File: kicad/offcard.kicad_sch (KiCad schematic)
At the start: 25 parts, among them J10 HeaderX4, J4 ScrewX2, J5 ScrewX4, J6 LCD, J7 HeaderX4, J8 ScrewX2, M1 12VDC motor, Q2 IRLML2502TRPbF, U3 NAU7802SGI

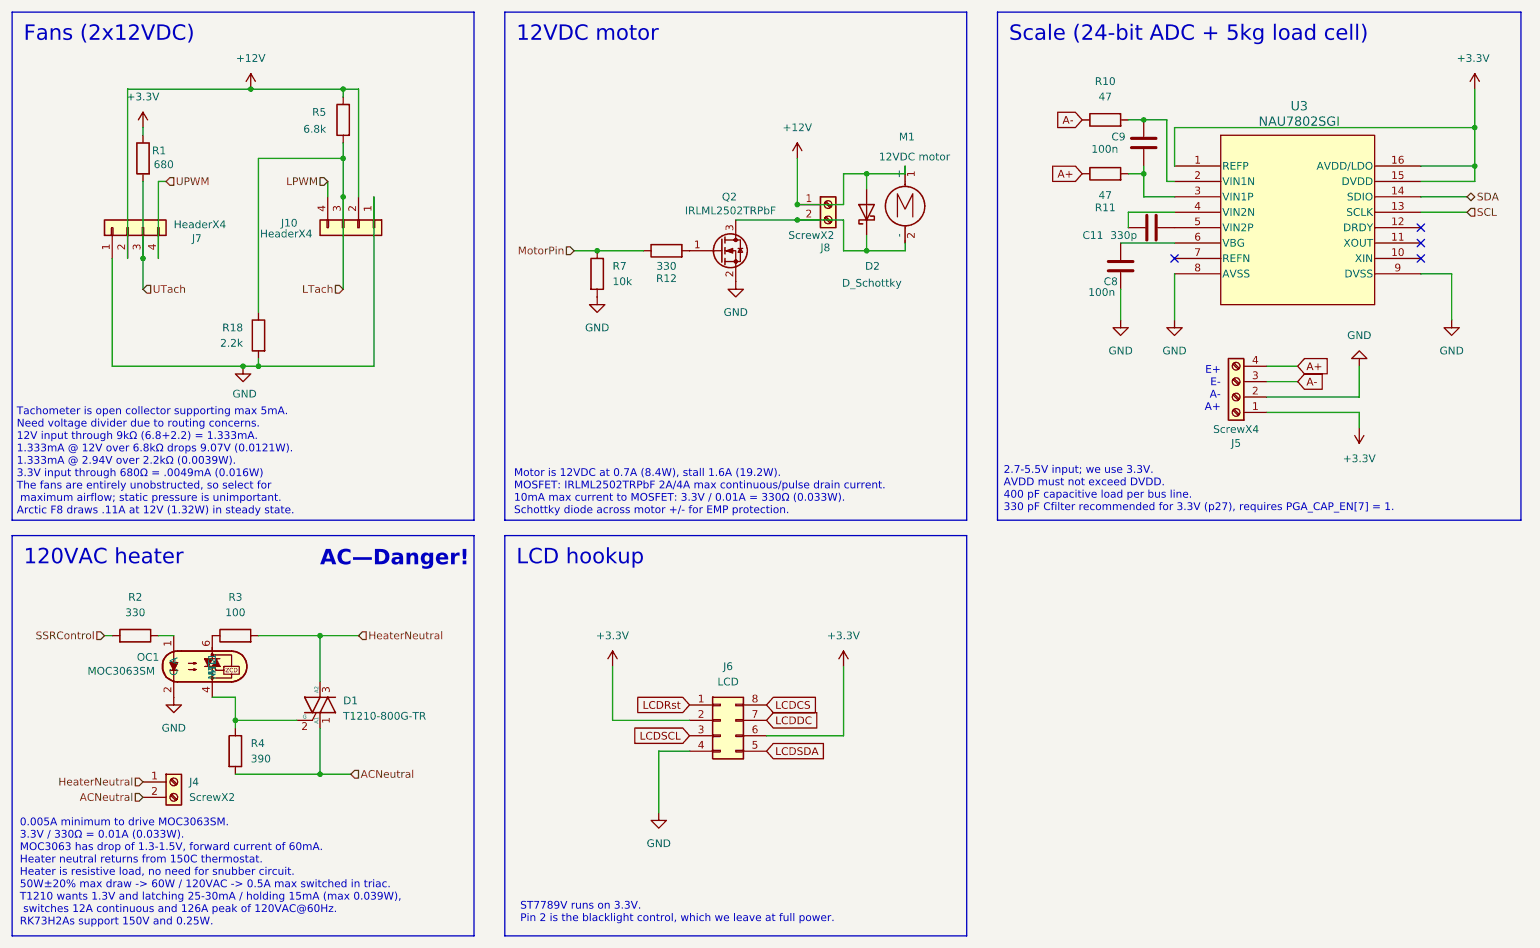
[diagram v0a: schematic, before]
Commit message: [nau7802] link avdd to refp, add capacitors #108
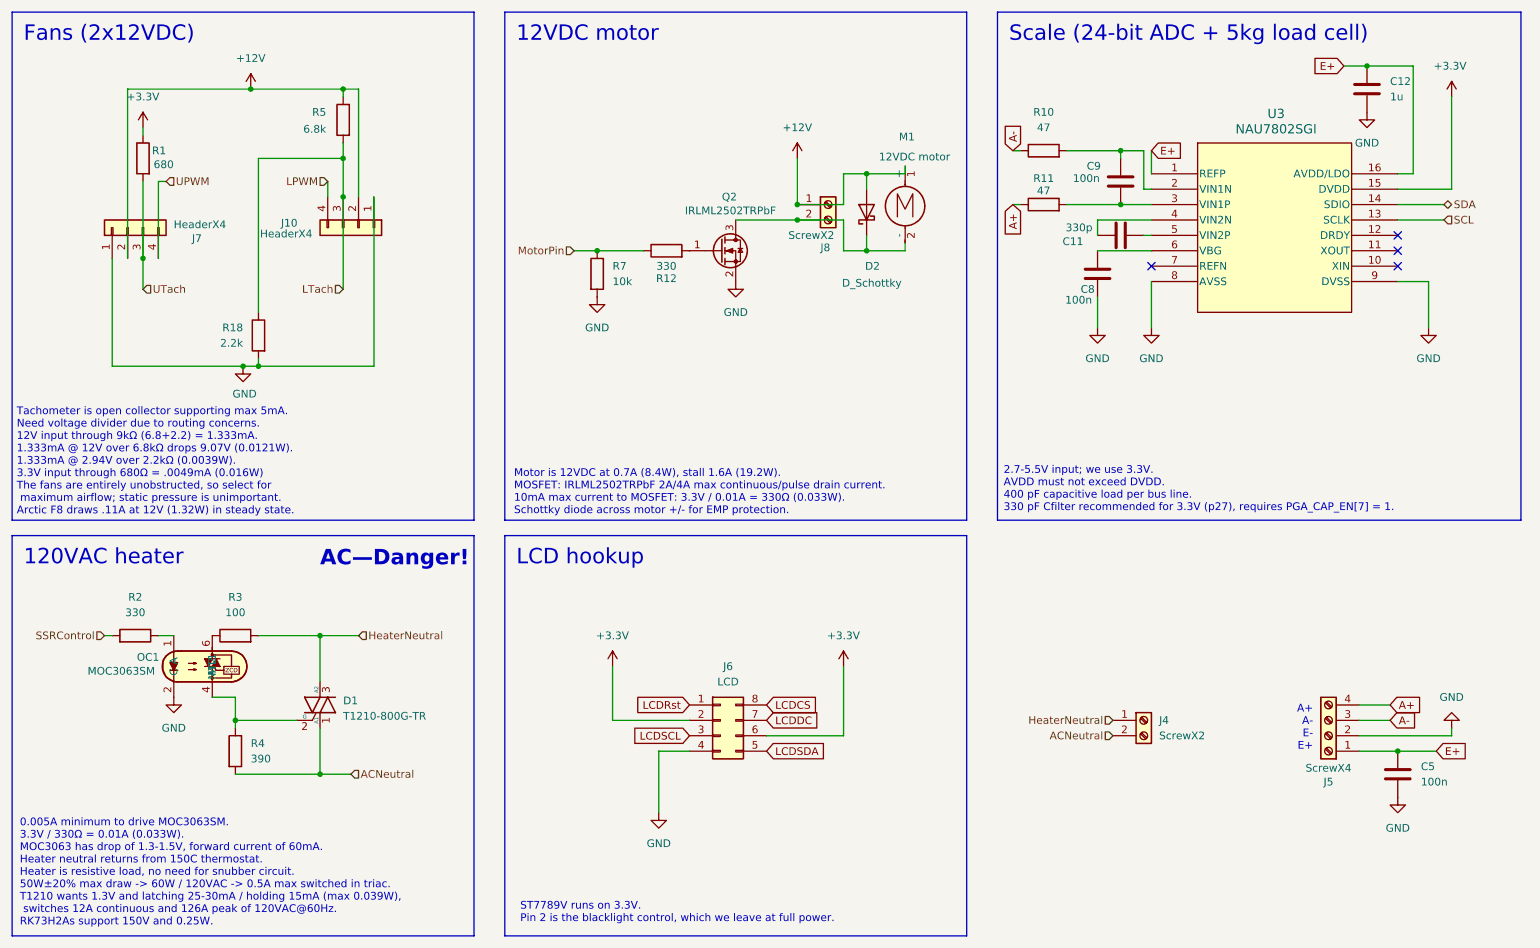
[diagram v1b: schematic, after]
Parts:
- added C12: 1u, Capacitor_SMD:C_1206_3216Metric_Pad1.33x1.80mm_HandSolder, symbol Device:C
- added C5: 100n, Capacitor_SMD:C_1206_3216Metric_Pad1.33x1.80mm_HandSolder, symbol Device:C
- R10, R11: footprint Resistor_SMD:R_0805_2012Metric_Pad1.20x1.40mm_HandSolder -> Resistor_SMD:R_1206_3216Metric_Pad1.30x1.75mm_HandSolder
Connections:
- net +3.3V: no longer J5.1 (Pin_1), U3.1 (REFP), U3.16 (AVDD/LDO)
- net GND: now also C12.2, C5.2
- new net E+: C12.1, C5.1, J5.1 (Pin_1), U3.1 (REFP), U3.16 (AVDD/LDO)
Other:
- note added: "A+ A- E- E+"
- note removed: "E+ E- A- A+"
- moved on the sheet: C11, C8, C9, J4, J5, R10, R11, U3

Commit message: move from lm35 to lmt87lpm
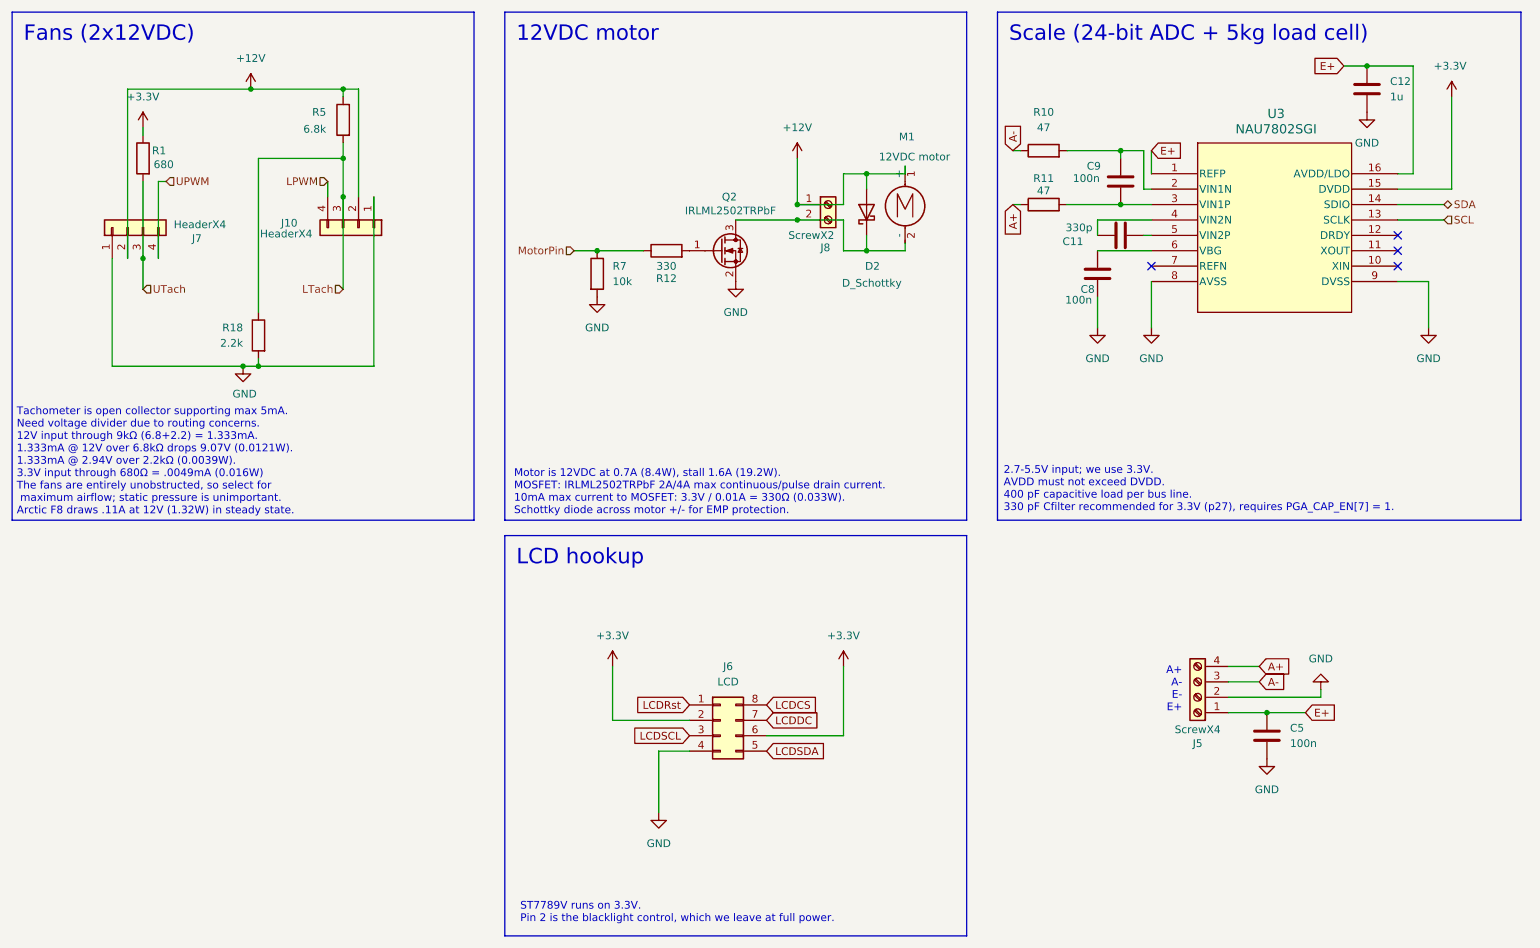
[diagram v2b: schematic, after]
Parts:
- removed D1: T1210-800G-TR, dank:T1210-800G-TR, symbol Triac_Thyristor:Generic_Triac_A1GA2
- removed J4: ScrewX2, TerminalBlock:TerminalBlock_bornier-2_P5.08mm, symbol Connector:Screw_Terminal_01x02
- removed OC1: MOC3063SM, dank:MOC306XS_LTO, symbol dank:MOC3063SM
- removed R2: 330, Resistor_SMD:R_1206_3216Metric_Pad1.30x1.75mm_HandSolder, symbol Device:R
- removed R3: 100, Resistor_SMD:R_1206_3216Metric_Pad1.30x1.75mm_HandSolder, symbol Device:R
- removed R4: 390, Resistor_SMD:R_1206_3216Metric_Pad1.30x1.75mm_HandSolder, symbol Device:R
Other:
- note removed: "0.005A minimum to drive MOC3063SM. 3.3V / 330Ω = 0.01A (0.033W). MOC3063 has drop of 1.3-1.5V, forward current of 60mA. Heater neutral returns from 150C thermostat. Heater is resistive load, no need for snubber circuit. 50W±20% max draw -> 60W / 120VAC -> 0.5A max switched in triac. T1210 wants 1.3V and latching 25-30mA / holding 15mA (max 0.039W), switches 12A continuous and 126A peak of 120VAC@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"
- note removed: "AC—Danger!"
- moved on the sheet: C5, J5

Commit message: [pcb] eliminate voltage divider before ltach closes #112
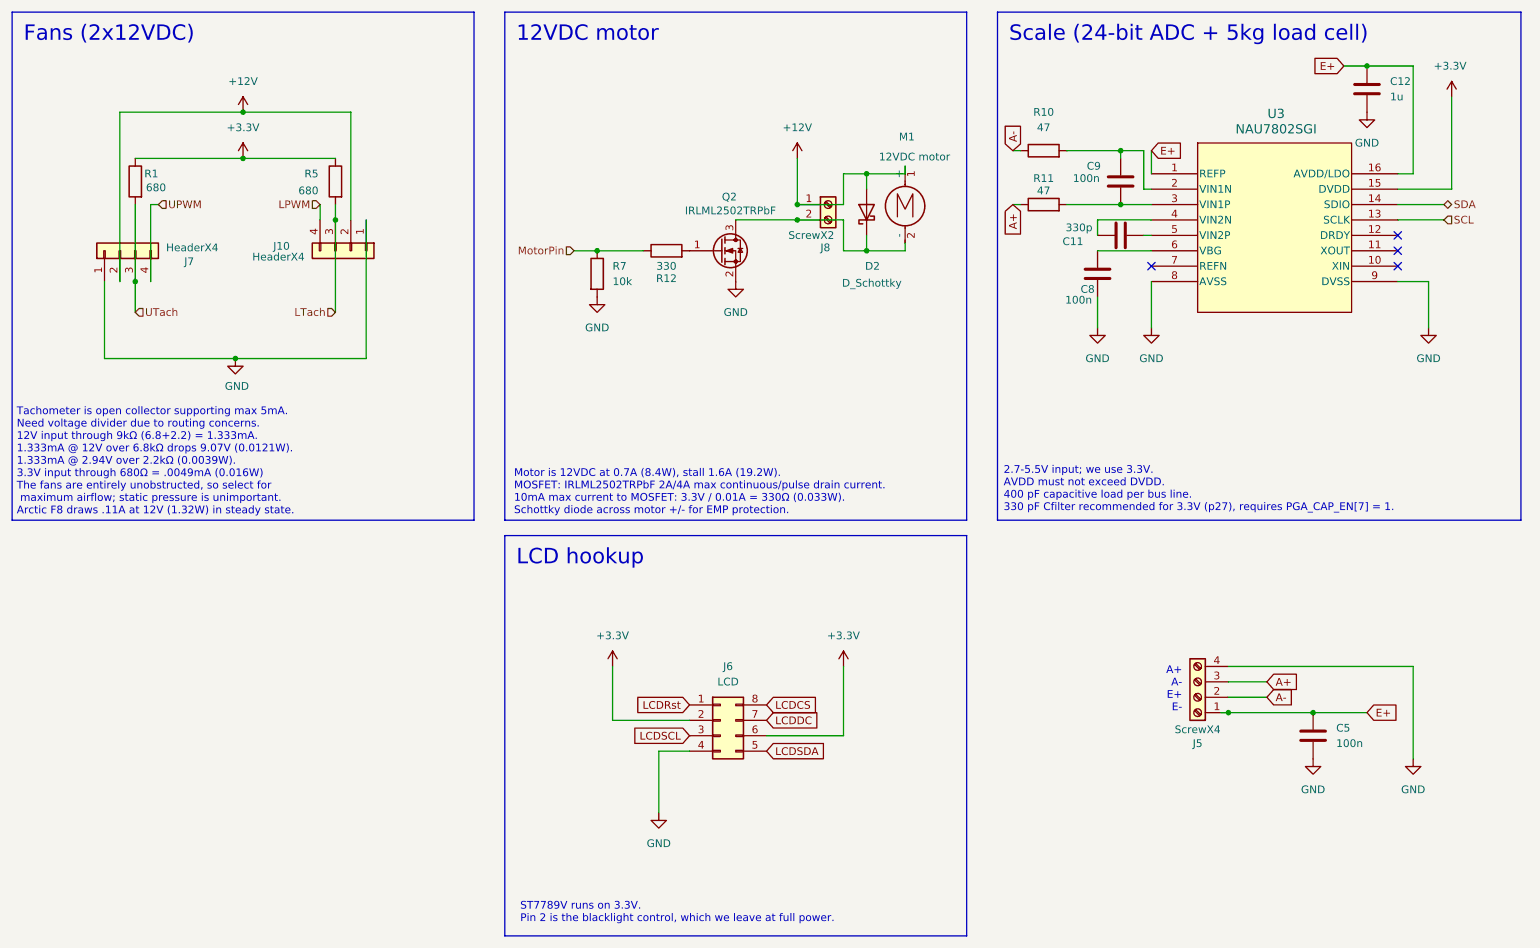
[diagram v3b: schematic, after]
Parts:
- removed R18: 2.2k, Resistor_SMD:R_1206_3216Metric_Pad1.30x1.75mm_HandSolder, symbol Device:R
- R5: value 6.8k -> 680
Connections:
- net +12V: no longer R5.1
- net +3.3V: now also R5.1
- net A+: now also J5.3 (Pin_3); no longer J5.4 (Pin_4)
- net A-: now also J5.2 (Pin_2); no longer J5.3 (Pin_3)
- net GND: now also J5.4 (Pin_4); no longer J5.2 (Pin_2)
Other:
- note added: "A+ A- E+ E-"
- note removed: "A+ A- E- E+"
- moved on the sheet: C5, J10, J7, R1, R5

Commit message: [pcb] label load cell hookups
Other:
- note added: "E- A+ A- E+"
- note removed: "A+ A- E+ E-"
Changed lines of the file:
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@@
 	(title_block
 		(title "dankdryer")
-		(date "2025-03-28")
-		(rev "2.1.9")
+		(date "2025-04-09")
+		(rev "2.2.0")
 		(company "dirty south supercomputing")
 		(comment 1 "nick black")
 	)
-	(text "A+\nA-\nE+\nE-"
+	(text "E-\nA+\nA-\nE+"
 		(exclude_from_sim no)
 		(at 208.28 129.54 0)

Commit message: kicad/scad v2.2.2
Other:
- note added: "Motor is 12VDC at 0.7A (8.4W), stall 1.6A (19.2W). MOSFET: IRLML2502TRPbF 2A/4A max continuous/pulse drain current. VDS: 20V VGS: ±12 RDS: 0.045Ω VTH: 1.2V Ci: 740pF Qg: 12nC. 10mA max current to MOSFET: 3.3V / 0.01A = 330Ω (0.033W). Schottky diode across motor +/- for EMP protection."
- note removed: "Motor is 12VDC at 0.7A (8.4W), stall 1.6A (19.2W). MOSFET: IRLML2502TRPbF 2A/4A max continuous/pulse drain current. 10mA max current to MOSFET: 3.3V / 0.01A = 330Ω (0.033W). Schottky diode across motor +/- for EMP protection."
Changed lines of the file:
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@@
 	(title_block
 		(title "dankdryer")
-		(date "2025-04-09")
-		(rev "2.2.0")
+		(date "2025-04-12")
+		(rev "2.2.1")
 		(company "dirty south supercomputing")
 		(comment 1 "nick black")
@@
 		)
 	)
-	(text "Motor is 12VDC at 0.7A (8.4W), stall 1.6A (19.2W).\nMOSFET: IRLML2502TRPbF 2A/4A max continuous/pulse drain current.\n10mA max current to MOSFET: 3.3V / 0.01A = 330Ω (0.033W).\nSchottky diode across motor +/- for EMP protection."
+	(text "Motor is 12VDC at 0.7A (8.4W), stall 1.6A (19.2W).\nMOSFET: IRLML2502TRPbF 2A/4A max continuous/pulse drain current.\nVDS: 20V VGS: ±12 RDS: 0.045Ω VTH: 1.2V Ci: 740pF Qg: 12nC.\n10mA max current to MOSFET: 3.3V / 0.01A = 330Ω (0.033W).\nSchottky diode across motor +/- for EMP protection."
 		(exclude_from_sim no)
-		(at 98.044 97.028 0)
+		(at 98.298 95.504 0)
 		(effects
 			(font

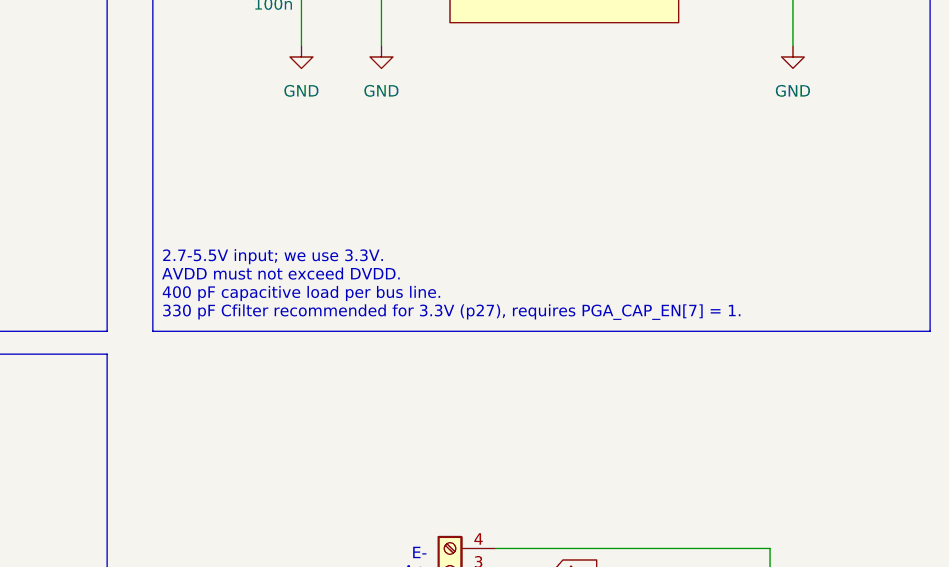
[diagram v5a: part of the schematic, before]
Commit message: kicad: mention AVDD/DVDD relation
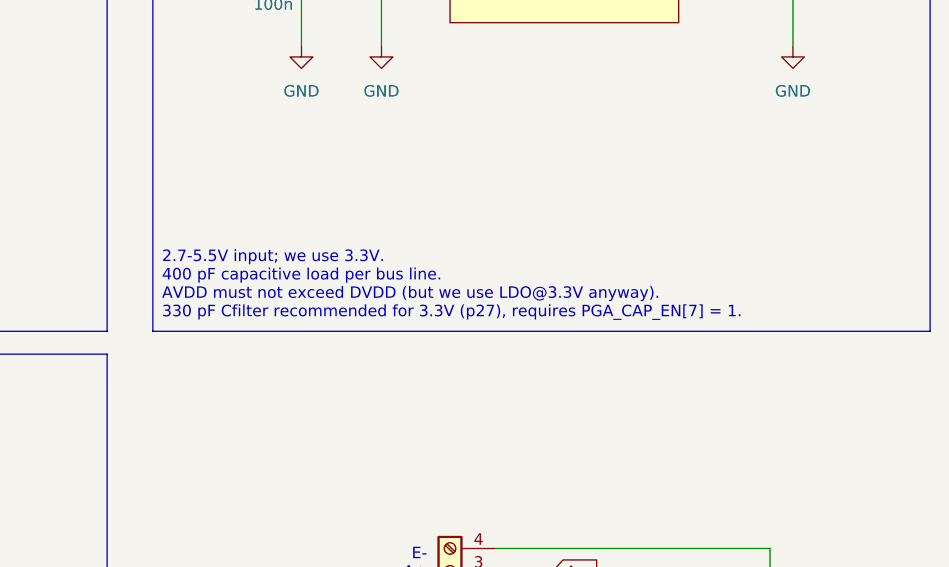
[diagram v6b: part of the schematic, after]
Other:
- note added: "2.7-5.5V input; we use 3.3V. 400 pF capacitive load per bus line. AVDD must not exceed DVDD (but we use LDO@3.3V anyway). 330 pF Cfilter recommended for 3.3V (p27), requires PGA_CAP_EN[7] = 1."
- note removed: "2.7-5.5V input; we use 3.3V. AVDD must not exceed DVDD. 400 pF capacitive load per bus line. 330 pF Cfilter recommended for 3.3V (p27), requires PGA_CAP_EN[7] = 1."
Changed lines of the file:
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@@
 		)
 	)
-	(text "2.7-5.5V input; we use 3.3V.\nAVDD must not exceed DVDD.\n400 pF capacitive load per bus line.\n330 pF Cfilter recommended for 3.3V (p27), requires PGA_CAP_EN[7] = 1."
+	(text "2.7-5.5V input; we use 3.3V.\n400 pF capacitive load per bus line.\nAVDD must not exceed DVDD (but we use LDO@3.3V anyway).\n330 pF Cfilter recommended for 3.3V (p27), requires PGA_CAP_EN[7] = 1."
 		(exclude_from_sim no)
 		(at 178.816 96.52 0)

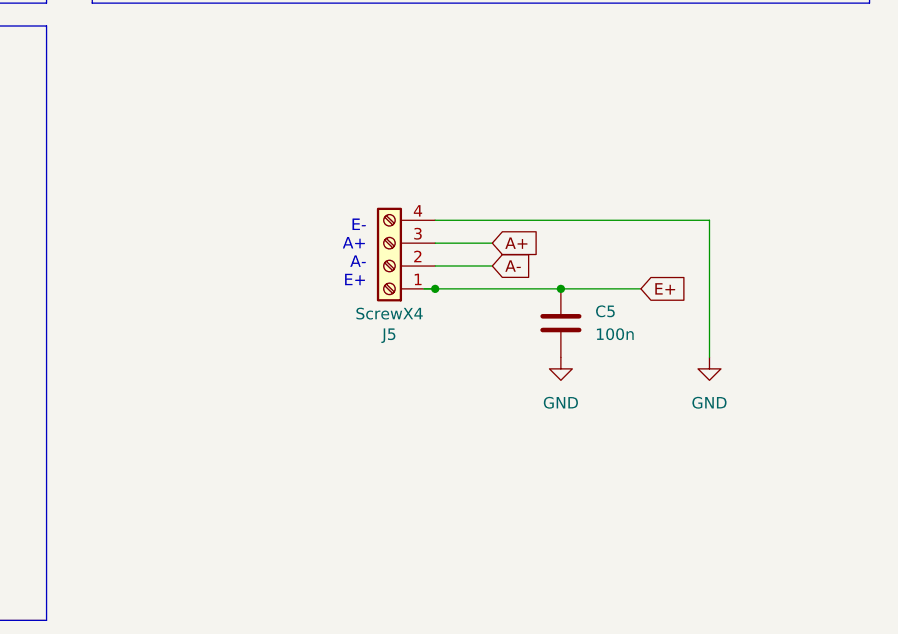
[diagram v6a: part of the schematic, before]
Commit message: [kicad] move to spring clips for load cell
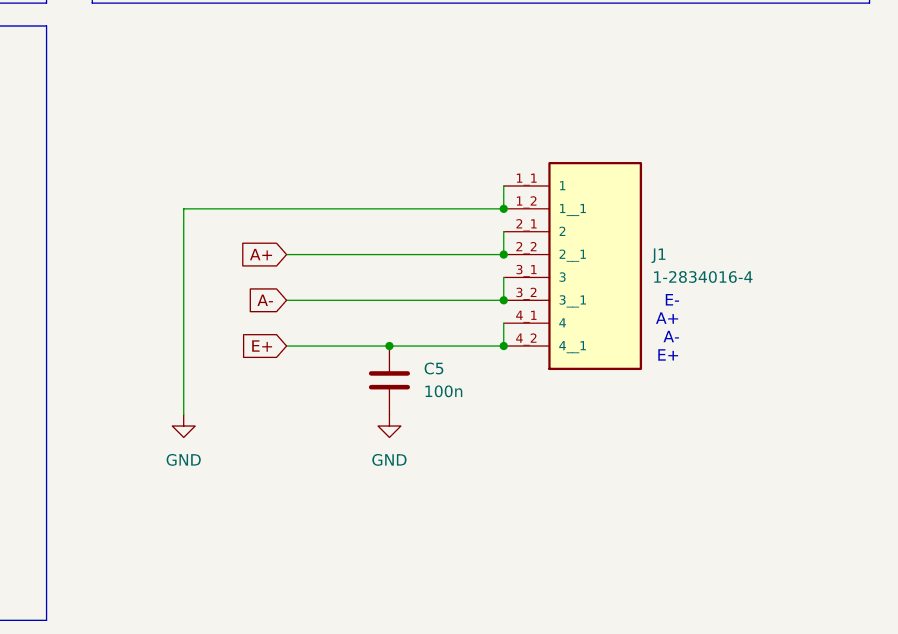
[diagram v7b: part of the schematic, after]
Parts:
- removed J5: ScrewX4, TerminalBlock:TerminalBlock_bornier-4_P5.08mm, symbol Connector:Screw_Terminal_01x04
- added J1: 1-2834016-4, dank:TE_1-2834016-4, symbol dank:1-2834016-4
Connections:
- net A+: now also J1.2_1 (2), J1.2_2 (2__1)
- net A-: now also J1.3_1 (3), J1.3_2 (3__1)
- net E+: now also J1.4_1 (4), J1.4_2 (4__1)
- net GND: now also J1.1_1 (1), J1.1_2 (1__1)
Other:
- moved on the sheet: C5
